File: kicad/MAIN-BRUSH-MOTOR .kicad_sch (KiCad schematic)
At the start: 6 parts, among them J11 MAIN BRUSH, Q10 AO3400

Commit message: Battery charging
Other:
- note added: "Isn't D18 reversed?"
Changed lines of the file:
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@@
+		)
+	)
+	(text "Isn't D18 reversed?"
+		(exclude_from_sim no)
+		(at 234.315 217.805 0)
+		(effects
+			(font
+				(size 1.27 1.27)
+			)
 		)
 	)

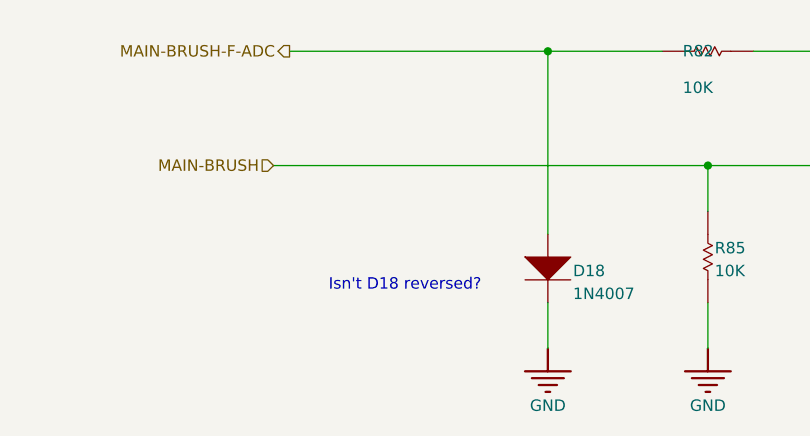
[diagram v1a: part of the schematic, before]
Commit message: Added Pi CM4/CM5
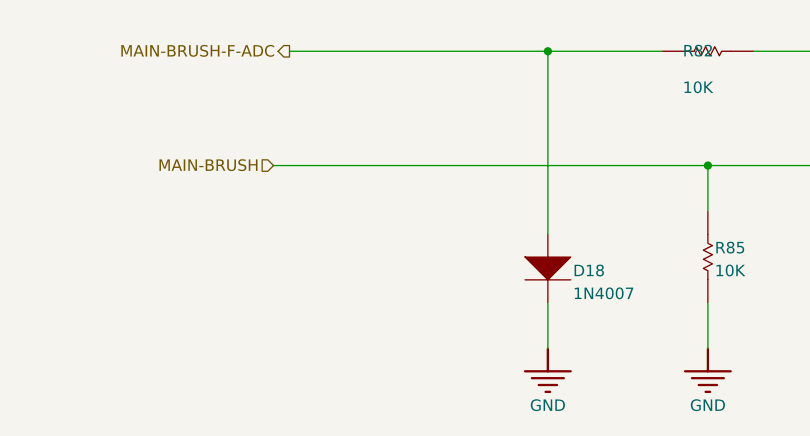
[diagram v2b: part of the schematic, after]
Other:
- note removed: "Isn't D18 reversed?"
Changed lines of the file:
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@@
-		)
-	)
-	(text "Isn't D18 reversed?"
-		(exclude_from_sim no)
-		(at 234.315 217.805 0)
-		(effects
-			(font
-				(size 1.27 1.27)
-			)
 		)
 	)
